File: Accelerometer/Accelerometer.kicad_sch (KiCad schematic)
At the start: 4 parts, among them U4 KX134-1211

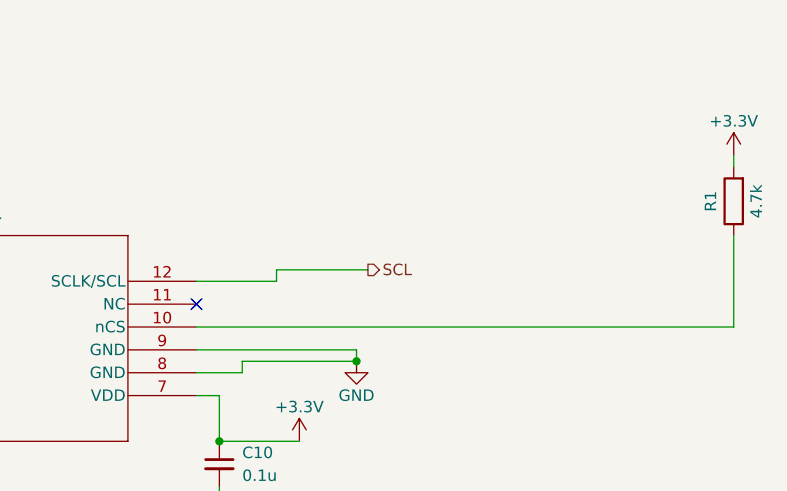
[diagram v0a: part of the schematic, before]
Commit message: Route sensors, IMU and radio board
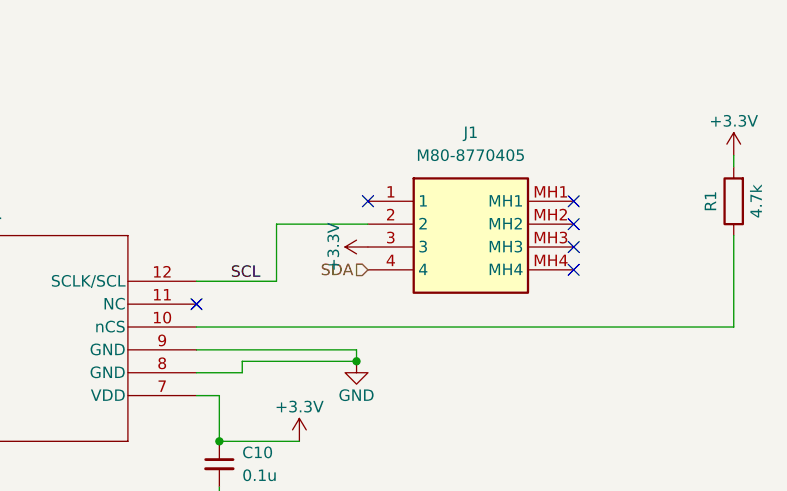
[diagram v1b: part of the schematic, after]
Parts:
- added J1: M80-8770405, M808770405, symbol M80-8770405:M80-8770405
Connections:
- net +3.3V: now also J1.3
- net SCL: now also J1.2
- net SDA: now also J1.4
- no-connect marks 3 -> 8
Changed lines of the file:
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@@
   (junction (at 165.1 109.22) (diameter 0) (color 0 0 0 0)
   )
+  (no_connect (at 204.47 85.09))
+  (no_connect (at 204.47 90.17))
+  (no_connect (at 181.61 82.55))
+  (no_connect (at 204.47 87.63))
   (no_connect (at 106.68 104.14))
   (no_connect (at 106.68 101.6))
+  (no_connect (at 204.47 82.55))
   (no_connect (at 162.56 93.98))
   (wire (pts (xy 105.41 99.06) (xy 106.68 99.06))
@@
     (stroke (width 0) (type default))
   )
-  (wire (pts (xy 171.45 90.17) (xy 181.61 90.17))
-    (stroke (width 0) (type default))
-  )
   (wire (pts (xy 107.95 67.31) (xy 107.95 68.58))
     (stroke (width 0) (type default))
@@
     (stroke (width 0) (type default))
   )
-  (wire (pts (xy 171.45 91.44) (xy 171.45 90.17))
+  (wire (pts (xy 171.45 85.09) (xy 171.45 91.44))
     (stroke (width 0) (type default))
   )
@@
     (stroke (width 0) (type default))
   )
-  (hierarchical_label "SCL" (shape output) (at 181.61 90.17 0) (fields_autoplaced)
-    (effects (font (size 1.27 1.27)) (justify left))
+  (wire (pts (xy 171.45 85.09) (xy 181.61 85.09))
+    (stroke (width 0) (type default))
+  )
+  (label "SCL" (at 166.37 91.44 0) (fields_autoplaced)
+    (effects (font (size 1.27 1.27)) (justify left bottom))
   )
   (hierarchical_label "SDA" (shape output) (at 92.71 92.71 180) (fields_autoplaced)
     (effects (font (size 1.27 1.27)) (justify right))
   )
+  (hierarchical_label "SDA" (shape input) (at 181.61 90.17 180) (fields_autoplaced)
+    (effects (font (size 1.27 1.27)) (justify right))
+  )
   (symbol (lib_id "power:+3.3V") (at 107.95 67.31 0) (unit 1)
     (in_bom yes) (on_board yes) (dnp no)
@@
     )
   )
+  (symbol (lib_id "M80-8770405:M80-8770405") (at 181.61 82.55 0) (unit 1)
+    (in_bom yes) (on_board yes) (dnp no) (fields_autoplaced)
+    (property "Reference" "J1" (at 193.04 74.93 0)
+      (effects (font (size 1.27 1.27)))
+    )
+    (property "Value" "M80-8770405" (at 193.04 77.47 0)
+      (effects (font (size 1.27 1.27)))
+    )
+    (property "Footprint" "M808770405" (at 200.66 177.47 0)
+      (effects (font (size 1.27 1.27)) (justify left top) hide)
+    )
+    (property "Datasheet" "https://cdn.harwin.com/pdfs/M80-877.pdf" (at 200.66 277.47 0)
+      (effects (font (size 1.27 1.27)) (justify left top) hide)
+    )
+    (property "Height" "5.56" (at 200.66 477.47 0)
+      (effects (font (size 1.27 1.27)) (justify left top) hide)
+    )
+    (property "Manufacturer_Name" "Harwin" (at 200.66 577.47 0)
+      (effects (font (size 1.27 1.27)) (justify left top) hide)
+    )
+    (property "Manufacturer_Part_Number" "M80-8770405" (at 200.66 677.47 0)
+      (effects (font (size 1.27 1.27)) (justify left top) hide)
+    )
+    (property "Mouser Part Number" "855-M80-8770405" (at 200.66 777.47 0)
+      (effects (font (size 1.27 1.27)) (justify left top) hide)
+    )
+    (property "Mouser Price/Stock" "https://www.mouser.co.uk/ProductDetail/Harwin/M80-8770405?qs=3tymCvhQ29ZPq83M%252Bf8kIA%3D%3D" (at 200.66 877.47 0)
+      (effects (font (size 1.27 1.27)) (justify left top) hide)
+    )
+    (property "Arrow Part Number" "" (at 200.66 977.47 0)
+      (effects (font (size 1.27 1.27)) (justify left top) hide)
+    )
+    (property "Arrow Price/Stock" "" (at 200.66 1077.47 0)
+      (effects (font (size 1.27 1.27)) (justify left top) hide)
+    )
+    (pin "1")
+    (pin "2")
+    (pin "3")
+    (pin "4")
+    (pin "MH1")
+    (pin "MH2")
+    (pin "MH3")
+    (pin "MH4")
+    (instances
+      (project "Accelerometer"
+        (path "/baa7c496-f9b6-450a-bc65-b627fb8a9223"
+          (reference "J1") (unit 1)
+        )
+      )
+    )
+  )
   (symbol (lib_id "Device:R") (at 222.25 82.55 180) (unit 1)
     (in_bom yes) (on_board yes) (dnp no)
@@
         )
       )
+    )
+  )
+  (symbol (lib_id "power:+3.3V") (at 181.61 87.63 90) (unit 1)
+    (in_bom yes) (on_board yes) (dnp no)
+    (property "Reference" "#PWR019" (at 185.42 87.63 0)
+      (effects (font (size 1.27 1.27)) hide)
+    )
+    (property "Value" "+3.3V" (at 177.8 87.63 0)
+      (effects (font (size 1.27 1.27)))
+    )
+    (property "Footprint" "" (at 181.61 87.63 0)
+      (effects (font (size 1.27 1.27)) hide)
+    )
+    (property "Datasheet" "" (at 181.61 87.63 0)
+      (effects (font (size 1.27 1.27)) hide)
+    )
+    (pin "1")
+    (instances
+      (project "Flight_Computer_V2"
+        (path "/39d7ebb3-b69d-4ae9-8f55-c9acfe77d345/4a05f57f-ad7d-4317-b08f-5601038a99f3"
+          (reference "#PWR019") (unit 1)
+        )
+        (path "/39d7ebb3-b69d-4ae9-8f55-c9acfe77d345/cb37c924-4cb5-4f3b-a39d-3b8b1b5d4537"
+          (reference "#PWR04") (unit 1)
+        )
+      )
+      (project "STM32F405RGT6"
+        (path "/6135eb53-87c0-4516-a6dc-aa2a3e58fdeb"
+          (reference "#PWR019") (unit 1)
+        )
+      )
+      (project "avionics_flight_computer"
+        (path "/b1d299c5-d712-4abd-abfc-85bf9dc0241e/1d0982b1-a7f8-42e4-83d7-31334d6351d0"
+          (reference "#PWR019") (unit 1)
+        )
+      )
+      (project "Accelerometer"
+        (path "/baa7c496-f9b6-450a-bc65-b627fb8a9223"
+          (reference "#PWR08") (unit 1)
+        )
+      )

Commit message: Done with most of the boards
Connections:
- net GND: now also J1.1
- no-connect marks 8 -> 7
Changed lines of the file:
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@@
   (no_connect (at 204.47 85.09))
   (no_connect (at 204.47 90.17))
-  (no_connect (at 181.61 82.55))
   (no_connect (at 204.47 87.63))
   (no_connect (at 106.68 104.14))
@@
     (stroke (width 0) (type default))
   )
+  (wire (pts (xy 175.26 82.55) (xy 181.61 82.55))
+    (stroke (width 0) (type default))
+  )
   (wire (pts (xy 167.64 100.33) (xy 180.34 100.33))
     (stroke (width 0) (type default))
@@
     (effects (font (size 1.27 1.27)) (justify right))
   )
+  (symbol (lib_id "power:GND") (at 175.26 82.55 270) (unit 1)
+    (in_bom yes) (on_board yes) (dnp no) (fields_autoplaced)
+    (property "Reference" "#PWR09" (at 168.91 82.55 0)
+      (effects (font (size 1.27 1.27)) hide)
+    )
+    (property "Value" "GND" (at 171.45 82.55 90)
+      (effects (font (size 1.27 1.27)) (justify right))
+    )
+    (property "Footprint" "" (at 175.26 82.55 0)
+      (effects (font (size 1.27 1.27)) hide)
+    )
+    (property "Datasheet" "" (at 175.26 82.55 0)
+      (effects (font (size 1.27 1.27)) hide)
+    )
+    (pin "1")
+    (instances
+      (project "Accelerometer"
+        (path "/baa7c496-f9b6-450a-bc65-b627fb8a9223"
+          (reference "#PWR09") (unit 1)
+        )
+      )
+    )
+  )
   (symbol (lib_id "power:+3.3V") (at 107.95 67.31 0) (unit 1)

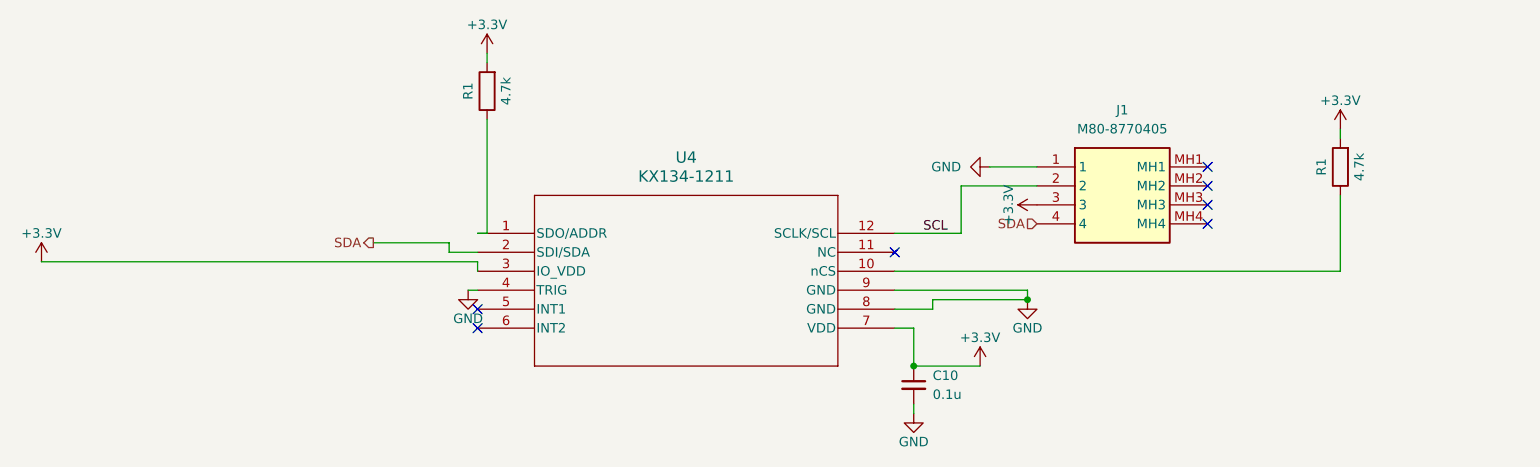
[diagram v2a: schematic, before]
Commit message: Fixed Accel, Barometer, FRAM, Inertia unit, and Magnetometer
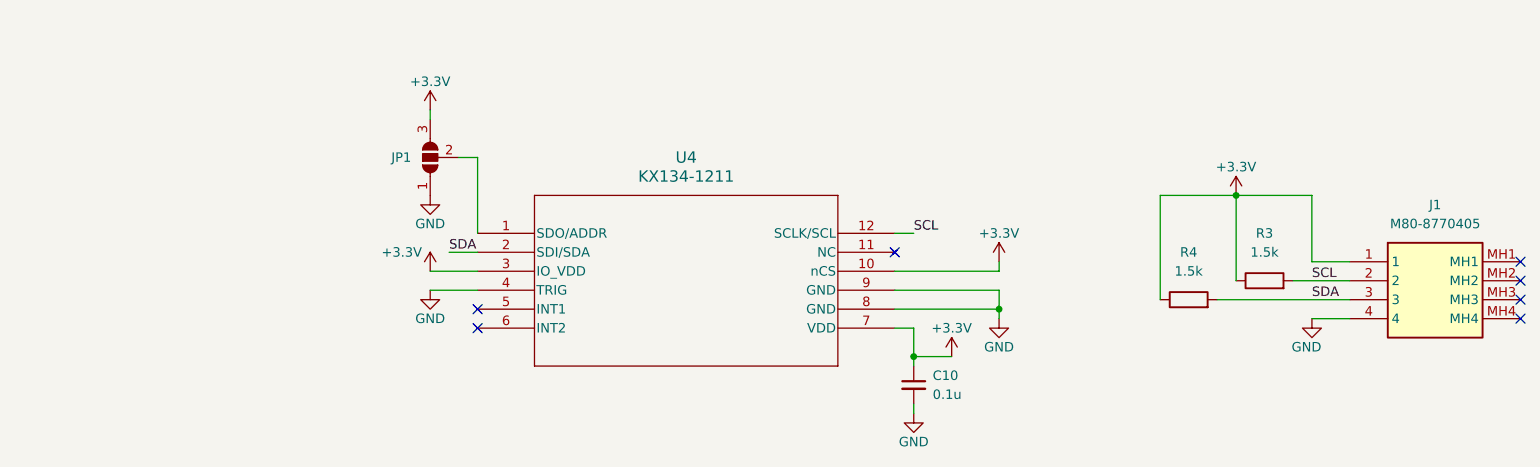
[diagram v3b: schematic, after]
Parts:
- removed R1 (x2): 4.7k, Resistor_SMD:R_0402_1005Metric, symbol Device:R
- added JP1: SolderJumper_3_Open, Jumper:SolderJumper-3_P1.3mm_Open_RoundedPad1.0x1.5mm_NumberLabels, symbol Jumper:SolderJumper_3_Open
- added R3, R4: 1.5k, Resistor_SMD:R_0201_0603Metric_Pad0.64x0.40mm_HandSolder, symbol Device:R
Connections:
- net +3.3V: now also J1.1, U4.10 (nCS), JP1.3 (B), R3.1, R4.1; no longer J1.3
- net GND: now also J1.4, JP1.1 (A); no longer J1.1
- net SCL: now also R3.2
- net SDA: now also J1.3, R4.2; no longer J1.4
- net at U4.1 (SDO/ADDR): now also JP1.2 (C)
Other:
- company: (none) -> USST Avionics
- title: (none) -> kx134 Accelerometer
- moved on the sheet: J1

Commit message: LC24 PCBs
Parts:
- removed J1: M80-8770405, M808770405, symbol M80-8770405:M80-8770405
- added C2, C3: 100nF, Capacitor_SMD:C_0402_1005Metric, symbol Device:C
- added C4, C5: 100n, Capacitor_SMD:C_0402_1005Metric, symbol Device:C_Small
- added C6: 2.2u, Capacitor_SMD:C_0603_1608Metric, symbol Device:C_Small
- added H1, H2, H3, H4: MountingHole_Pad, Mounting_Wuerth:Mounting_Wuerth_WA-SMSI-M1.6_H1mm_9774010633, symbol Mechanical:MountingHole_Pad
- added IC1: FRAM, MB85RC256VPF_G_JNERE2:FPT-8P-M08_FUJ, symbol LibraryLoader:MB85RC256VPF-G-JNERE2
- added IC2: BMI088, BMI088:QFN_BMI085_BOS, symbol LibraryLoader:BMI088
- added IC3: MMC5603NJ, MMC5603NJ:WLP4_0P82X0P82_MEM, symbol LibraryLoader:MMC5603NJ
- added J2: M80-8770422, Harwin-M80-8770422:CONN_M80-87704_HRW, symbol Harwin-M80-8770422:M80-8770422
- added JP2, JP6, JP7: SolderJumper_3_Open, Jumper:SolderJumper-3_P1.3mm_Open_RoundedPad1.0x1.5mm_NumberLabels, symbol Jumper:SolderJumper_3_Open
- added JP3, JP4, JP5, JP8: SolderJumper_2_Open, Jumper:SolderJumper-2_P1.3mm_Open_RoundedPad1.0x1.5mm, symbol Jumper:SolderJumper_2_Open
- added U2: BMP280, Package_LGA:Bosch_LGA-8_2x2.5mm_P0.65mm_ClockwisePinNumbering, symbol Sensor_Pressure:BMP280
- U4: footprint XDCR_KX003-1077:XDCR_KX003-1077 -> KX134:LGA12_2X2X0P9_ROM
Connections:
- net +3.3V: now also C2.1, C3.1, C4.1, C5.1, C6.1, IC1.8 (VDD), IC2.11 (VDDIO), IC2.3 (VDD), IC2.7 (PS), IC3.B1 (VDD), J2.1, JP2.3 (B), JP3.1 (A), JP4.1 (A), JP5.1 (A), JP6.3 (B), JP7.3 (B), JP8.1 (A), U2.6 (VDDIO), U2.8 (VDD)
- net GND: now also C2.2, C3.2, C4.2, C5.2, C6.2, H1.1, H2.1, H3.1, H4.1, IC1.4 (VSS), IC1.7 (WP), IC2.2 (NC), IC2.4 (GNDA), IC2.6 (GNDIO), IC3.A1 (VSA), J2.4, JP2.1 (A), JP6.1 (A), JP7.1 (A), U2.1 (GND), U2.7 (GND)
- net SCL: now also IC1.6 (SCL), IC2.8 (SCL/SCK), IC3.A2 (SCL), J2.2, U2.4 (SCK)
- net SDA: now also IC1.5 (SDA), IC2.9 (SDA/SDI), IC3.B2 (SDA), J2.3, U2.3 (SDI)
- new net: JP2.2 (C), U2.5 (SDO)
- new net: IC1.1 (A0), JP4.2 (B)
- new net: IC1.2 (A1), JP3.2 (B)
- new net: IC1.3 (A2), JP5.2 (B)
- new net: IC2.10 (SDO2), JP7.2 (C)
- new net: IC2.15 (SDO1), JP6.2 (C)
- new net: JP8.2 (B), U2.2 (CSB)
- no-connect marks 7 -> 9
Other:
- moved on the sheet: C10, JP1, R3, R4, U4
